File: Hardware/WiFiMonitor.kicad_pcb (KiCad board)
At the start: 2 copper layers, 47.2 x 47.1 mm, 39 parts, among them J1 ADAP_ESP, J3 BATT, J5 FTDI, U1 4N25, U2 4N25, U3 4N25, U4 4N25, U5 MCP73831T, U6 AP1117-33, U7 DS3231MZ+

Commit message: Fix vias and stuff FTW
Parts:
- moved D2 7.13 mm to (149.8, 72.1), turned to 90 degrees
- moved D4 4.17 mm to (142.3, 78.5)
- moved R16 3.07 mm to (158.3, 79.7)
- moved D3 0.93 mm to (142.3, 75.9)
- moved J3 0.78 mm to (144.7, 71.0)
- moved C2 0.77 mm to (160.2, 79.6)
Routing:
- net +3V3: track 142.4 -> 156.6 mm, vias 9 -> 11
- net VCC: track 52.1 -> 40.6 mm
- net Net-(C1-Pad1): track 33.5 -> 22.1 mm, vias 2 -> 1
- net Net-(R4-Pad1): track 19.5 -> 29.7 mm
- net Net-(D2-Pad1): track 15.5 -> 24.3 mm
- net Net-(R1-Pad1): track 45.1 -> 51.5 mm
- net /BAT: track 32.6 -> 26.5 mm
- net /D3: track 69.9 -> 75.4 mm
- net /D2: track 73.3 -> 78.3 mm
- net GNDA: track 88.7 -> 84.1 mm
- net Net-(R3-Pad1): track 37.5 -> 41.9 mm
- net Net-(IN4-Pad1): track 29.8 -> 33.3 mm
- net GND: track 158.6 -> 161.5 mm, vias 5 -> 6
- net /D0: track 85.2 -> 87.4 mm
- net /D1: track 67.7 -> 66.1 mm
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
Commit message: Added logo EC
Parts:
- added G***: LOGO, TIH:electronic_cats_logo_4x3, F.Cu at (141.0, 102.0)
- added G***: LOGO, TIH:electronic_cats_logo_8x6, B.Cu at (163.5, 104.5)
- renumbered COMUN1 to COM1, COMUN2 to COM2

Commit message: Auto stash before merge of "HARDWARER" and "origin/HARDWARER"
6 PINES FTDI
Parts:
- removed J5: FTDI, Pin_Headers:Pin_Header_Straight_1x05_Pitch2.54mm
- added J2: FTDI, Pin_Headers:Pin_Header_Straight_1x06_Pitch2.54mm, F.Cu at (131.2, 78.2)
- U5: value MCP73831T -> U5
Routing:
- net /TX: track 23.1 -> 25.0 mm
- net VCC: track 40.6 -> 39.4 mm
- net /RX: track 23.1 -> 24.2 mm
- net GND: track 161.5 -> 160.9 mm

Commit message: Pista_near
Move
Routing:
- net +3V3: track 156.6 -> 157.5 mm
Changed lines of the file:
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@@
     (links 70)
     (no_connects 0)
-    (area 126.056132 67.439999 173.398541 114.790001)
+    (area 125.549999 67.068854 174.355 116.145)
     (thickness 1.6)
     (drawings 28)
-    (tracks 631)
+    (tracks 633)
     (zones 0)
     (modules 41)
@@
   (segment (start 144.11 76.04) (end 143.94 75.87) (width 0.5) (layer B.Cu) (net 4))
   (via (at 145.89 76.04) (size 1.2) (drill 0.6) (layers F.Cu B.Cu) (net 4))
+  (segment (start 157.81 87.19) (end 163.34 87.19) (width 0.5) (layer B.Cu) (net 5))
+  (segment (start 163.34 87.19) (end 163.35 87.18) (width 0.5) (layer B.Cu) (net 5))
+  (segment (start 156.63 87.737003) (end 157.642997 87.737003) (width 0.5) (layer F.Cu) (net 5))
+  (segment (start 156.142997 87.737003) (end 156.63 87.737003) (width 0.5) (layer F.Cu) (net 5))
+  (segment (start 156.63 87.737003) (end 157.262997 87.737003) (width 0.5) (layer F.Cu) (net 5))
+  (segment (start 157.262997 87.737003) (end 157.81 87.19) (width 0.5) (layer F.Cu) (net 5))
+  (via (at 157.81 87.19) (size 1.2) (drill 0.6) (layers F.Cu B.Cu) (net 5))
   (segment (start 150.41 83.05) (end 150.41 84.4) (width 0.5) (layer F.Cu) (net 5))
   (segment (start 150.41 84.4) (end 154.14 88.13) (width 0.5) (layer F.Cu) (net 5))
   (segment (start 154.14 88.13) (end 155.75 88.13) (width 0.5) (layer F.Cu) (net 5))
   (segment (start 155.75 88.13) (end 156.142997 87.737003) (width 0.5) (layer F.Cu) (net 5))
-  (segment (start 156.142997 87.737003) (end 157.642997 87.737003) (width 0.5) (layer F.Cu) (net 5))
-  (segment (start 157.642997 87.737003) (end 158.26 87.12) (width 0.5) (layer F.Cu) (net 5))
-  (segment (start 163.35 87.18) (end 158.32 87.18) (width 0.5) (layer B.Cu) (net 5))
-  (segment (start 158.32 87.18) (end 158.26 87.12) (width 0.5) (layer B.Cu) (net 5))
-  (via (at 158.26 87.12) (size 1.2) (drill 0.6) (layers F.Cu B.Cu) (net 5))
   (segment (start 164.71 89.92) (end 163.35 88.56) (width 0.5) (layer F.Cu) (net 5))
   (segment (start 163.35 88.56) (end 163.35 87.18) (width 0.5) (layer F.Cu) (net 5))

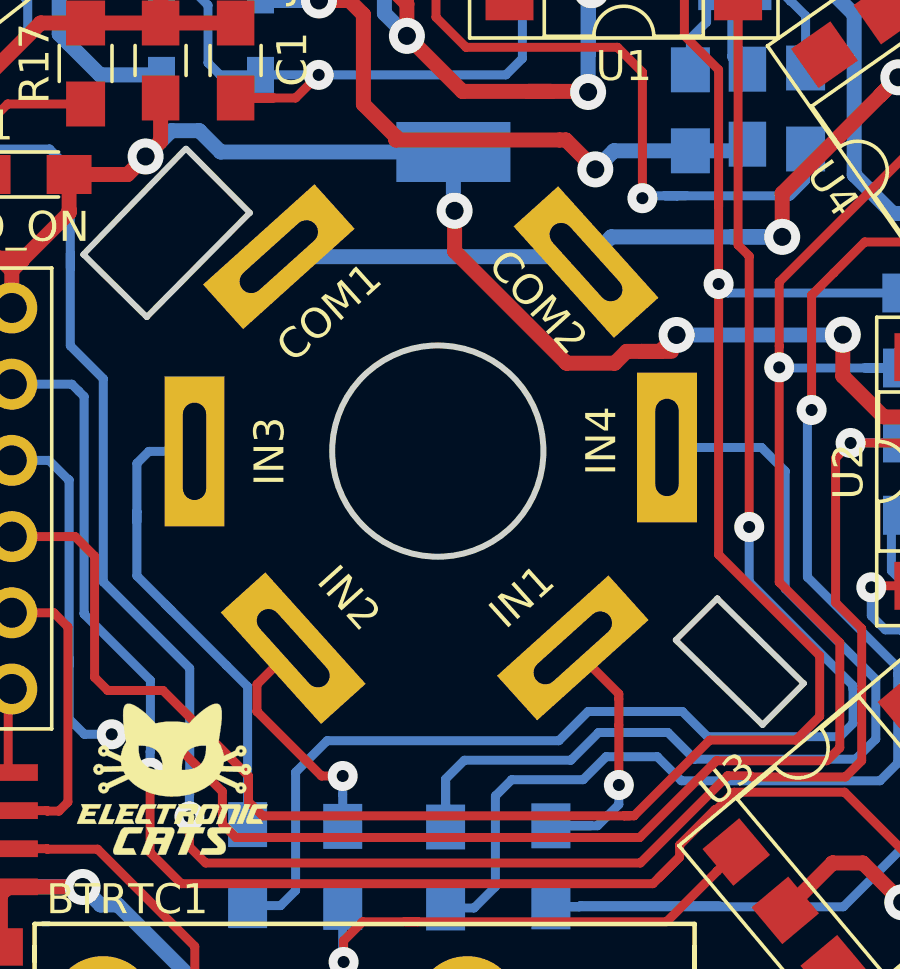
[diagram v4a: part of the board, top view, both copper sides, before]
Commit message: pads_in
move
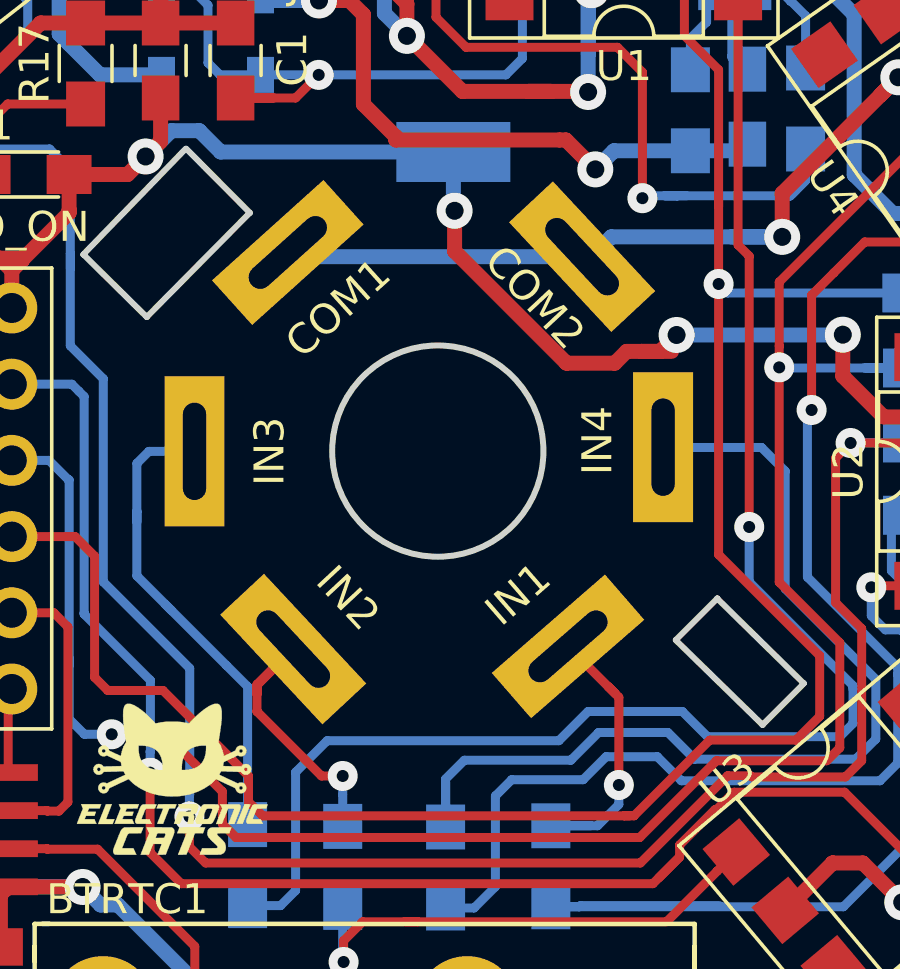
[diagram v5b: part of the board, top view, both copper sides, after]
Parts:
- moved COM1 0.33 mm to (144.8, 84.4)
- moved COM2 0.22 mm to (154.7, 84.6), turned to 133 degrees
- moved IN1 0.17 mm to (154.2, 97.6), turned to 41 degrees
- moved IN4 0.13 mm to (157.4, 90.9)
- turned IN2 to 133 degrees
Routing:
- net Net-(IN2-Pad1): track 8.04 -> 10.0 mm
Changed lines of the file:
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@@
     (thickness 1.6)
     (drawings 28)
-    (tracks 633)
+    (tracks 636)
     (zones 0)
     (modules 41)
@@
     (visible_elements 7FFFFFFF)
     (pcbplotparams
-      (layerselection 0x00030_80000001)
-      (usegerberextensions false)
+      (layerselection 0x011fc_80000001)
+      (usegerberextensions true)
       (excludeedgelayer true)
       (linewidth 0.100000)
@@
       (outputformat 1)
       (mirror false)
-      (drillshape 1)
+      (drillshape 0)
       (scaleselection 1)
       (outputdirectory ""))
@@
   )
   (module PADS:PAD_4X2mmTH (layer F.Cu)
-    (at 154.35 97.62 42)
-    (fp_text reference IN1 (at -0.119133 -2.4083 42) (layer F.SilkS)
+    (at 154.19 97.57 41)
+    (fp_text reference IN1 (at -0.119133 -2.4083 41) (layer F.SilkS)
       (effects (font (size 1 1) (thickness 0.15)))
     )
-    (fp_text value 0_IN (at 0 -2.5 42) (layer F.Fab)
+    (fp_text value 0_IN (at 0 -2.5 41) (layer F.Fab)
       (effects (font (size 1 1) (thickness 0.15)))
     )
-    (pad 1 thru_hole rect (at 0 0 42) (size 5 2) (drill oval 3.25 0.78) (layers *.Cu *.Mask)
+    (pad 1 thru_hole rect (at 0 0 41) (size 5 2) (drill oval 3.25 0.78) (layers *.Cu *.Mask)
       (net 10 "Net-(IN1-Pad1)"))
   )
   (module PADS:PAD_4X2mmTH (layer F.Cu)
-    (at 145.03 97.63 132)
-    (fp_text reference IN2 (at 0 2.5 132) (layer F.SilkS)
+    (at 145.03 97.66 133)
+    (fp_text reference IN2 (at 0 2.5 133) (layer F.SilkS)
       (effects (font (size 1 1) (thickness 0.15)))
     )
-    (fp_text value 1_IN (at 0 -2.5 132) (layer F.Fab)
+    (fp_text value 1_IN (at 0 -2.5 133) (layer F.Fab)
       (effects (font (size 1 1) (thickness 0.15)))
     )
-    (pad 1 thru_hole rect (at 0 0 132) (size 5 2) (drill oval 3.25 0.78) (layers *.Cu *.Mask)
+    (pad 1 thru_hole rect (at 0 0 133) (size 5 2) (drill oval 3.25 0.78) (layers *.Cu *.Mask)
       (net 11 "Net-(IN2-Pad1)"))
   )
@@
   )
   (module PADS:PAD_4X2mmTH (layer F.Cu)
-    (at 157.49 90.94 90)
+    (at 157.36 90.93 90)
     (fp_text reference IN4 (at 0.22 -2.19 90) (layer F.SilkS)
       (effects (font (size 1 1) (thickness 0.15)))
@@
   )
   (module PADS:PAD_4X2mmTH (layer F.Cu)
-    (at 144.55 84.58 42)
+    (at 144.85 84.44 42)
     (fp_text reference COM1 (at 0 2.5 42) (layer F.SilkS)
       (effects (font (size 1 1) (thickness 0.15)))
@@
   )
   (module PADS:PAD_4X2mmTH (layer F.Cu)
-    (at 154.79 84.76 132)
-    (fp_text reference COM2 (at 0.082226 -2.078975 132) (layer F.SilkS)
+    (at 154.66 84.58 133)
+    (fp_text reference COM2 (at 0.082226 -2.078975 133) (layer F.SilkS)
       (effects (font (size 1 1) (thickness 0.15)))
     )
-    (fp_text value TORRETA (at 0 -2.5 132) (layer F.Fab)
+    (fp_text value TORRETA (at 0 -2.5 133) (layer F.Fab)
       (effects (font (size 1 1) (thickness 0.15)))
     )
-    (pad 1 thru_hole rect (at 0 0 132) (size 5 2) (drill oval 3.25 0.78) (layers *.Cu *.Mask)
+    (pad 1 thru_hole rect (at 0 0 133) (size 5 2) (drill oval 3.25 0.78) (layers *.Cu *.Mask)
       (net 6 GNDA))
   )
@@
   (via (at 127.76 84.63) (size 1.2) (drill 0.6) (layers F.Cu B.Cu) (net 5))
   (via (at 126.95 94.56) (size 1.2) (drill 0.6) (layers F.Cu B.Cu) (net 5))
-  (segment (start 144.55 84.58) (end 154.61 84.58) (width 0.5) (layer B.Cu) (net 6))
+  (segment (start 154.66 84.58) (end 144.99 84.58) (width 0.5) (layer B.Cu) (net 6))
+  (segment (start 144.99 84.58) (end 144.85 84.44) (width 0.5) (layer B.Cu) (net 6))
   (segment (start 154.61 84.58) (end 154.79 84.76) (width 0.5) (layer B.Cu) (net 6))
   (segment (start 161.33 83.92) (end 161.33 82.47) (width 0.5) (layer F.Cu) (net 6))
@@
   (segment (start 162.11 82.04) (end 162.11 80.99) (width 0.3) (layer B.Cu) (net 9))
   (segment (start 162.11 81.483998) (end 162.11 80.99) (width 0.3) (layer B.Cu) (net 9))
-  (segment (start 155.885 100.195) (end 155.885 99.32) (width 0.3) (layer F.Cu) (net 10))
-  (segment (start 155.885 99.32) (end 155.885 99.155) (width 0.3) (layer F.Cu) (net 10))
-  (segment (start 155.885 99.155) (end 154.35 97.62) (width 0.3) (layer F.Cu) (net 10))
-  (segment (start 155.885 102.19) (end 155.885 100.195) (width 0.3) (layer F.Cu) (net 10))
+  (segment (start 155.775 99.155) (end 155.53 98.91) (width 0.3) (layer F.Cu) (net 10))
+  (segment (start 155.53 98.91) (end 154.19 97.57) (width 0.3) (layer F.Cu) (net 10))
+  (segment (start 155.885 102.19) (end 155.885 99.265) (width 0.3) (layer F.Cu) (net 10))
+  (segment (start 155.885 99.265) (end 155.53 98.91) (width 0.3) (layer F.Cu) (net 10))
   (segment (start 155.175 103.55) (end 155.885 102.84) (width 0.3) (layer B.Cu) (net 10))
   (segment (start 155.885 102.84) (end 155.885 102.19) (width 0.3) (layer B.Cu) (net 10))
@@
   (segment (start 153.62 103.55) (end 155.175 103.55) (width 0.3) (layer B.Cu) (net 10))
   (segment (start 153.62 103.55) (end 154.95 103.55) (width 0.3) (layer B.Cu) (net 10))
-  (segment (start 143.822894 99.74) (end 143.822894 98.837106) (width 0.3) (layer F.Cu) (net 11))
+  (segment (start 143.822894 99.16) (end 143.822894 98.837106) (width 0.3) (layer F.Cu) (net 11))
+  (segment (start 143.822894 99.74) (end 143.822894 99.16) (width 0.3) (layer F.Cu) (net 11))
+  (segment (start 143.822894 99.16) (end 143.822894 98.867106) (width 0.3) (layer F.Cu) (net 11))
+  (segment (start 143.822894 98.867106) (end 145.03 97.66) (width 0.3) (layer F.Cu) (net 11))
   (segment (start 143.822894 98.837106) (end 145.03 97.63) (width 0.3) (layer F.Cu) (net 11))
   (segment (start 145.972894 101.89) (end 143.822894 99.74) (width 0.3) (layer F.Cu) (net 11))
@@
   (segment (start 161.43 91.73) (end 160.64 90.94) (width 0.3) (layer B.Cu) (net 13))
   (segment (start 160.64 90.94) (end 157.49 90.94) (width 0.3) (layer B.Cu) (net 13))
-  (segment (start 157.56 91.01) (end 157.49 90.94) (width 0.3) (layer F.Cu) (net 13))
   (segment (start 150.11 103.59) (end 150.11 102.09) (width 0.3) (layer B.Cu) (net 13))
   (segment (start 141.57 103.24) (end 141.57 104.25) (width 0.3) (layer F.Cu) (net 14))

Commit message: pads2
move
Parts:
- moved IN2 0.89 mm to (145.9, 97.7), turned to 145 degrees
- moved COM1 0.44 mm to (145.3, 84.5), turned to 40 degrees
- moved COM2 0.11 mm to (154.6, 84.7)
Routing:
- net Net-(IN2-Pad1): track 10.0 -> 7.86 mm
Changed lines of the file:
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@@
     (area 125.549999 67.068854 174.355 116.145)
     (thickness 1.6)
-    (drawings 28)
-    (tracks 636)
+    (drawings 30)
+    (tracks 632)
     (zones 0)
     (modules 41)
@@
     (add_net VCC)
   )
+  (module PADS:PAD_4X2mmTH (layer F.Cu)
+    (at 145.92 97.67 145)
+    (fp_text reference IN2 (at 0 2.5 145) (layer F.SilkS)
+      (effects (font (size 1 1) (thickness 0.15)))
+    )
+    (fp_text value 1_IN (at 0 -2.5 145) (layer F.Fab)
+      (effects (font (size 1 1) (thickness 0.15)))
+    )
+    (pad 1 thru_hole rect (at 0 0 145) (size 5 2) (drill oval 3.25 0.78) (layers *.Cu *.Mask)
+      (net 11 "Net-(IN2-Pad1)"))
+  )
   (module TO_SOT_Packages_SMD:SOT-223-3_TabPin2 (layer B.Cu)
     (at 150.37 77.94 270)
@@
   )
   (module PADS:PAD_4X2mmTH (layer F.Cu)
-    (at 145.03 97.66 133)
-    (fp_text reference IN2 (at 0 2.5 133) (layer F.SilkS)
-      (effects (font (size 1 1) (thickness 0.15)))
-    )
-    (fp_text value 1_IN (at 0 -2.5 133) (layer F.Fab)
-      (effects (font (size 1 1) (thickness 0.15)))
-    )
-    (pad 1 thru_hole rect (at 0 0 133) (size 5 2) (drill oval 3.25 0.78) (layers *.Cu *.Mask)
-      (net 11 "Net-(IN2-Pad1)"))
-  )
-  (module PADS:PAD_4X2mmTH (layer F.Cu)
     (at 141.74 91.07 90)
     (fp_text reference IN3 (at 0 2.5 90) (layer F.SilkS)
@@
   )
   (module PADS:PAD_4X2mmTH (layer F.Cu)
-    (at 144.85 84.44 42)
-    (fp_text reference COM1 (at 0 2.5 42) (layer F.SilkS)
+    (at 145.29 84.49 40)
+    (fp_text reference COM1 (at 0 2.5 40) (layer F.SilkS)
       (effects (font (size 1 1) (thickness 0.15)))
     )
-    (fp_text value NC (at 0 -2.5 42) (layer F.Fab)
+    (fp_text value NC (at 0 -2.5 40) (layer F.Fab)
       (effects (font (size 1 1) (thickness 0.15)))
     )
-    (pad 1 thru_hole rect (at 0 0 42) (size 5 2) (drill oval 3.25 0.78) (layers *.Cu *.Mask)
+    (pad 1 thru_hole rect (at 0 0 40) (size 5 2) (drill oval 3.25 0.78) (layers *.Cu *.Mask)
       (net 6 GNDA))
   )
   (module PADS:PAD_4X2mmTH (layer F.Cu)
-    (at 154.66 84.58 133)
+    (at 154.59 84.66 133)
     (fp_text reference COM2 (at 0.082226 -2.078975 133) (layer F.SilkS)
       (effects (font (size 1 1) (thickness 0.15)))
@@
     )
   )
+  (dimension 10.120835 (width 0.3) (layer Margin)
+    (gr_text "10.121 mm" (at 150.245462 94.674818 0.7359724973) (layer Margin)
+      (effects (font (size 1.5 1.5) (thickness 0.3)))
+    )
+    (feature1 (pts (xy 145.21 96.65) (xy 145.168122 93.38993)))
+    (feature2 (pts (xy 155.33 96.52) (xy 155.288122 93.25993)))
+    (crossbar (pts (xy 155.322803 95.959707) (xy 145.202803 96.089707)))
+    (arrow1a (pts (xy 145.202803 96.089707) (xy 146.321681 95.488865)))
+    (arrow1b (pts (xy 145.202803 96.089707) (xy 146.336746 96.66161)))
+    (arrow2a (pts (xy 155.322803 95.959707) (xy 154.18886 95.387804)))
+    (arrow2b (pts (xy 155.322803 95.959707) (xy 154.203925 96.560549)))
+  )
+  (dimension 5.11 (width 0.3) (layer Margin)
+    (gr_text "5 mm" (at 150.435 96.56) (layer Margin)
+      (effects (font (size 1.5 1.5) (thickness 0.3)))
+    )
+    (feature1 (pts (xy 147.88 98.58) (xy 147.88 95.21)))
+    (feature2 (pts (xy 152.99 98.58) (xy 152.99 95.21)))
+    (crossbar (pts (xy 152.99 97.91) (xy 147.88 97.91)))
+    (arrow1a (pts (xy 147.88 97.91) (xy 149.006504 97.323579)))
+    (arrow1b (pts (xy 147.88 97.91) (xy 149.006504 98.496421)))
+    (arrow2a (pts (xy 152.99 97.91) (xy 151.863496 97.323579)))
+    (arrow2b (pts (xy 152.99 97.91) (xy 151.863496 98.496421)))
+  )
   (gr_circle (center 149.85 91.06) (end 151.05 94.37) (layer Edge.Cuts) (width 0.2))
   (gr_circle (center 149.86 91.03) (end 153.19 93.27) (layer Margin) (width 0.2))
@@
   (segment (start 153.62 103.55) (end 155.175 103.55) (width 0.3) (layer B.Cu) (net 10))
   (segment (start 153.62 103.55) (end 154.95 103.55) (width 0.3) (layer B.Cu) (net 10))
-  (segment (start 143.822894 99.16) (end 143.822894 98.837106) (width 0.3) (layer F.Cu) (net 11))
-  (segment (start 143.822894 99.74) (end 143.822894 99.16) (width 0.3) (layer F.Cu) (net 11))
-  (segment (start 143.822894 99.16) (end 143.822894 98.867106) (width 0.3) (layer F.Cu) (net 11))
-  (segment (start 143.822894 98.867106) (end 145.03 97.66) (width 0.3) (layer F.Cu) (net 11))
-  (segment (start 143.822894 98.837106) (end 145.03 97.63) (width 0.3) (layer F.Cu) (net 11))
-  (segment (start 145.972894 101.89) (end 143.822894 99.74) (width 0.3) (layer F.Cu) (net 11))
-  (segment (start 143.822894 99.74) (end 143.822894 99.732894) (width 0.3) (layer F.Cu) (net 11))
+  (segment (start 145.972894 101.89) (end 144.44 100.357106) (width 0.3) (layer F.Cu) (net 11))
+  (segment (start 144.44 100.357106) (end 144.44 99.15) (width 0.3) (layer F.Cu) (net 11))
+  (segment (start 144.44 99.15) (end 145.92 97.67) (width 0.3) (layer F.Cu) (net 11))
   (segment (start 146.68 101.89) (end 145.972894 101.89) (width 0.3) (layer F.Cu) (net 11))
   (via (at 146.68 101.89) (size 1) (drill 0.4) (layers F.Cu B.Cu) (net 11))
